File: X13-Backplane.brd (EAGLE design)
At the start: 101.6 x 139.3 mm, 38 parts, among them J1 PXC-PTSM-04-RA-1778641, J2 284512-4, J3 284512-8, J4 PXC-PTSM-04-RA-1778641, J5 PXC-PTSM-04-RA-1778641, J6 284512-4, J8 284512-8, T1 284512-3, T2 284512-3, T3 284512-3, T4 284512-3, T5 284512-3, T6 284512-3, T7 284512-3, T8 284512-3

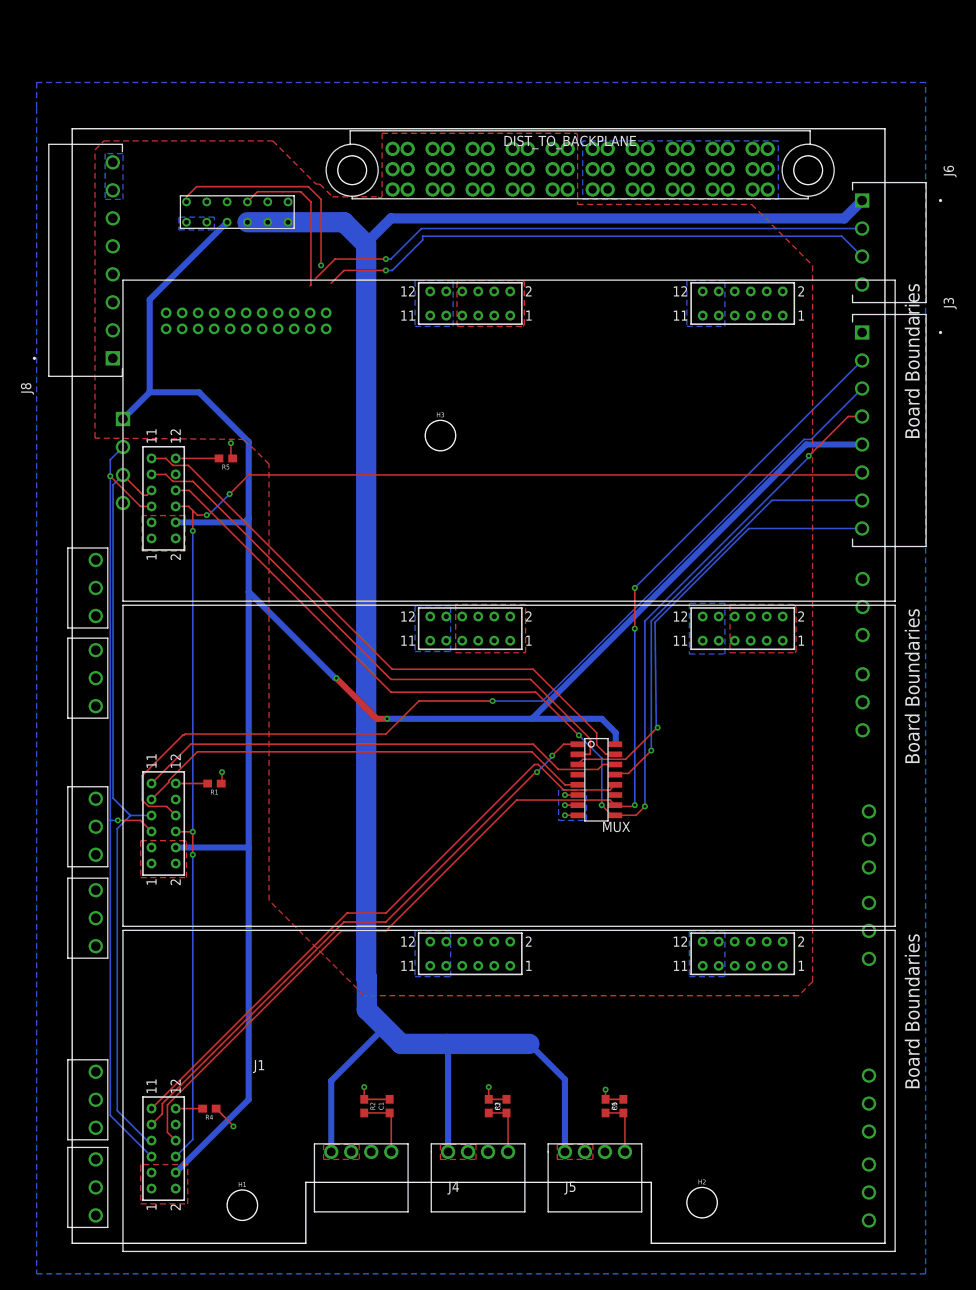
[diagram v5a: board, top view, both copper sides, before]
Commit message: updated board layout and connections
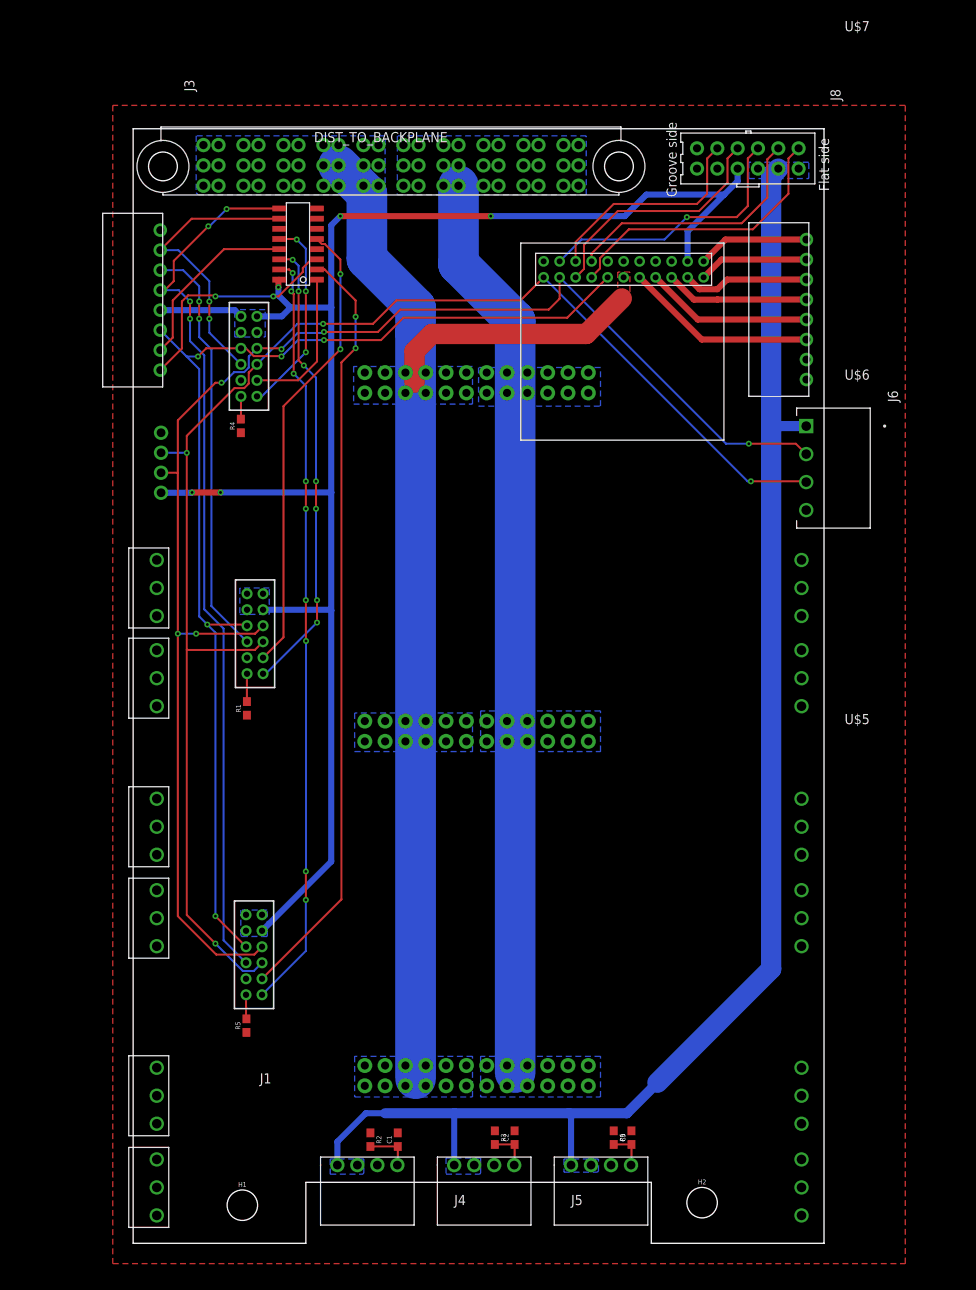
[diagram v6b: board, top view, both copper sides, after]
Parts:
- removed H3: 6-32-HOLE, Mounting Holes:6-32-HOLE
- added U$5, U$6, U$7: BACKPLANE_ESC_ADAPTER_PWRBKP, Backplane_ESC_adapter:BACKPLANE_ESC_ADAPTER_BKP_PWR
- DIST_LOGIC_TO_BACKPLANE: value IPL1-107-01-L-D-RE-P -> IPL1-106-01-L-D-K; device Backplane_Dist_Logic_Connector:IPL1-107-01-L-D-RE-P -> Backplane_Dist_Logic_Connector:IPL1-106-01-L-D-K
- J2: value 284512-4 -> PXC-PTSM-04-RA-1778641; device 284512-4:TE_284512-4 -> Phoenix Contact PTSM-04-V-1778573:PXC-PTSM-04-RA-1778641
- J3, J8: value 284512-8 -> PXC-8-RA-1778683; device 284512-8:TE_284512-8 -> Phoenix Contact PTSM 8 pin:PXC-8-RA-1778683
- U$1, U$2, U$3: value BACKPLANE_CONNECTORS -> BACKPLANE_CONNECTORSBKP; device BLHeli_32 45A:BACKPLANE_CONNECTORS -> BLHeli_32 45A:BACKPLANE_CONNECTORS_BKP
- moved U$3 101.8 mm to (22.7, 36.1)
- moved J3 98.7 mm to (3.81, 128.7)
- moved U$1 96.9 mm to (22.1, 110.9)
- moved R4 85.4 mm to (21.1, 102.2), turned to 90 degrees
- moved J8 79.6 mm to (84.6, 127.6), turned to 270 degrees
- moved R5 70.9 mm to (21.8, 27.2), turned to 90 degrees
- moved MUX 66.6 mm to (30.6, 120.5), turned to 180 degrees
- moved DIST_LOGIC_TO_BACKPLANE 64.2 mm to (90.8, 134.3)
- moved U$2 61.0 mm to (22.9, 76.2)
- moved U$4 47.9 mm to (78.9, 122.7), flipped to the top, turned to 180 degrees
- moved T2 35.3 mm to (93.2, 40.6)
- moved MC4 33.2 mm to (93.2, 6.99)
- moved J6 29.0 mm to (91.8, 96.9)
- moved DIST_TO_BACKPLANE 23.7 mm to (39.8, 139.5)
- moved R1 10.2 mm to (21.8, 66.9), turned to 90 degrees
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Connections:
- new net 12VGND: DIST_TO_BACKPLANE.1@1, DIST_TO_BACKPLANE.1@2, DIST_TO_BACKPLANE.1@3, DIST_TO_BACKPLANE.1@4, DIST_TO_BACKPLANE.1@5, DIST_TO_BACKPLANE.1@6, DIST_TO_BACKPLANE.2@1, DIST_TO_BACKPLANE.2@2, DIST_TO_BACKPLANE.2@3, DIST_TO_BACKPLANE.2@4, DIST_TO_BACKPLANE.2@5, DIST_TO_BACKPLANE.2@6, DIST_TO_BACKPLANE.3@1, DIST_TO_BACKPLANE.3@2, DIST_TO_BACKPLANE.3@3, DIST_TO_BACKPLANE.3@4, DIST_TO_BACKPLANE.3@5, DIST_TO_BACKPLANE.3@6, DIST_TO_BACKPLANE.4@1, DIST_TO_BACKPLANE.4@2, DIST_TO_BACKPLANE.4@3, DIST_TO_BACKPLANE.4@4, DIST_TO_BACKPLANE.4@5, DIST_TO_BACKPLANE.4@6, DIST_TO_BACKPLANE.5@1, DIST_TO_BACKPLANE.5@2, DIST_TO_BACKPLANE.5@3, DIST_TO_BACKPLANE.5@4, DIST_TO_BACKPLANE.5@5, DIST_TO_BACKPLANE.5@6, U$5.GND@1, U$5.GND@10, U$5.GND@11, U$5.GND@12, U$5.GND@2, U$5.GND@3, U$5.GND@4, U$5.GND@5, U$5.GND@6, U$5.GND@7, U$5.GND@8, U$5.GND@9, U$6.GND@1, U$6.GND@10, U$6.GND@11, U$6.GND@12, U$6.GND@2, U$6.GND@3, U$6.GND@4, U$6.GND@5, U$6.GND@6, U$6.GND@7, U$6.GND@8, U$6.GND@9, U$7.GND@1, U$7.GND@10, U$7.GND@11, U$7.GND@12, U$7.GND@2, U$7.GND@3, U$7.GND@4, U$7.GND@5, U$7.GND@6, U$7.GND@7, U$7.GND@8, U$7.GND@9
- net 12V: now also U$5.12V@1, U$5.12V@10, U$5.12V@11, U$5.12V@12, U$5.12V@2, U$5.12V@3, U$5.12V@4, U$5.12V@5, U$5.12V@6, U$5.12V@7, U$5.12V@8, U$5.12V@9, U$6.12V@1, U$6.12V@10, U$6.12V@11, U$6.12V@12, U$6.12V@2, U$6.12V@3, U$6.12V@4, U$6.12V@5, U$6.12V@6, U$6.12V@7, U$6.12V@8, U$6.12V@9, U$7.12V@1, U$7.12V@10, U$7.12V@11, U$7.12V@12, U$7.12V@2, U$7.12V@3, U$7.12V@4, U$7.12V@5, U$7.12V@6, U$7.12V@7, U$7.12V@8, U$7.12V@9; no longer U$1.1, U$1.13, U$1.14, U$1.15, U$1.16, U$1.17, U$1.18, U$1.19, U$1.2, U$1.20, U$1.3, U$1.4, U$1.5, U$1.6, U$1.7, U$1.8, U$2.1, U$2.13, U$2.14, U$2.15, U$2.16, U$2.17, U$2.18, U$2.19, U$2.2, U$2.20, U$2.3, U$2.4, U$2.5, U$2.6, U$2.7, U$2.8, U$3.1, U$3.13, U$3.14, U$3.15, U$3.16, U$3.17, U$3.18, U$3.19, U$3.2, U$3.20, U$3.3, U$3.4, U$3.5, U$3.6, U$3.7, U$3.8
- net 3.3V: now also U$1.1, U$1.2, U$1.3, U$1.4, U$2.1, U$2.2, U$2.3, U$2.4, U$3.1, U$3.2, U$3.3, U$3.4; no longer U$1.25, U$1.26, U$1.27, U$1.28, U$2.25, U$2.26, U$2.27, U$2.28, U$3.25, U$3.26, U$3.27, U$3.28
- net CAN_H: now also U$1.5, U$2.5, U$3.5; no longer U$1.29, U$2.29, U$3.29
- net CAN_L: now also U$1.7, U$2.7, U$3.7; no longer U$1.31, U$2.31, U$3.31
- net ESCID_1: now also U$1.12; no longer U$1.36
- net ESCID_2: now also U$2.12; no longer U$2.36
- net ESCID_3: now also U$3.12; no longer U$3.36
- net GND: no longer DIST_TO_BACKPLANE.1@1, DIST_TO_BACKPLANE.1@2, DIST_TO_BACKPLANE.1@3, DIST_TO_BACKPLANE.1@4, DIST_TO_BACKPLANE.1@5, DIST_TO_BACKPLANE.1@6, DIST_TO_BACKPLANE.2@1, DIST_TO_BACKPLANE.2@2, DIST_TO_BACKPLANE.2@3, DIST_TO_BACKPLANE.2@4, DIST_TO_BACKPLANE.2@5, DIST_TO_BACKPLANE.2@6, DIST_TO_BACKPLANE.3@1, DIST_TO_BACKPLANE.3@2, DIST_TO_BACKPLANE.3@3, DIST_TO_BACKPLANE.3@4, DIST_TO_BACKPLANE.3@5, DIST_TO_BACKPLANE.3@6, DIST_TO_BACKPLANE.4@1, DIST_TO_BACKPLANE.4@2, DIST_TO_BACKPLANE.4@3, DIST_TO_BACKPLANE.4@4, DIST_TO_BACKPLANE.4@5, DIST_TO_BACKPLANE.4@6, DIST_TO_BACKPLANE.5@1, DIST_TO_BACKPLANE.5@2, DIST_TO_BACKPLANE.5@3, DIST_TO_BACKPLANE.5@4, DIST_TO_BACKPLANE.5@5, DIST_TO_BACKPLANE.5@6, U$1.10, U$1.11, U$1.12, U$1.21, U$1.22, U$1.23, U$1.24, U$1.9, U$2.10, U$2.11, U$2.12, U$2.21, U$2.22, U$2.23, U$2.24, U$2.9, U$3.10, U$3.11, U$3.12, U$3.21, U$3.22, U$3.23, U$3.24, U$3.9
- net NRST: now also U$1.6, U$2.6, U$3.6; no longer U$1.30, U$2.30, U$3.30
- net PROG_1: now also U$1.8; no longer U$1.32
- net PROG_2: now also U$2.8; no longer U$2.32
- net PROG_3: now also U$3.8; no longer U$3.32
- net SWCLK_1: now also U$1.11; no longer U$1.35
- net SWCLK_2: now also U$2.11; no longer U$2.35
- net SWCLK_3: now also U$3.11; no longer U$3.35
- net SWDIO_1: now also U$1.9; no longer U$1.33
- net SWDIO_2: now also U$2.9; no longer U$2.33
- net SWDIO_3: now also U$3.9; no longer U$3.33
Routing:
- net 12V: track 0.00 -> 152.4 mm
- net 12VGND: track 0.00 -> 113.8 mm
- net PROG_1: track 146.8 -> 36.3 mm, vias 3 -> 2
- net PROG_2: track 118.1 -> 52.6 mm, vias 1 -> 2
- net 5V: track 244.2 -> 183.9 mm
- net 3.3V: track 268.5 -> 210.8 mm, vias 2 -> 5
- net SWDIO_1: track 73.8 -> 18.8 mm, vias 2 -> 0
- net SWCLK_1: track 77.3 -> 25.2 mm, vias 0 -> 3
- net C2_2: track 0.00 -> 35.9 mm
- net C2_1: track 0.00 -> 32.6 mm
- net SWCLK_IN: track 54.6 -> 22.8 mm, vias 1 -> 0
- net ALERT_2: track 0.00 -> 30.5 mm
- net PROG_3: track 140.4 -> 110.5 mm
- net NRST: track 172.3 -> 144.1 mm
- net ALERT_1: track 0.00 -> 27.6 mm
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- added copper zone on layer 16, net 12V
- added copper zone on layer 16, net 12VGND
- added copper zone on layer 16, net 3.3V
- added copper zone on layer 16, net 5V
- added copper zone on layer 1, net GND
- removed copper zone on layer 1, net 3.3V
- removed copper zone on layer 1, net 5V
- removed copper zone on layer 16, net GND
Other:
- board size 101.6 x 139.3 mm -> 86.4 x 139.3 mm

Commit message: updated board layout and connections
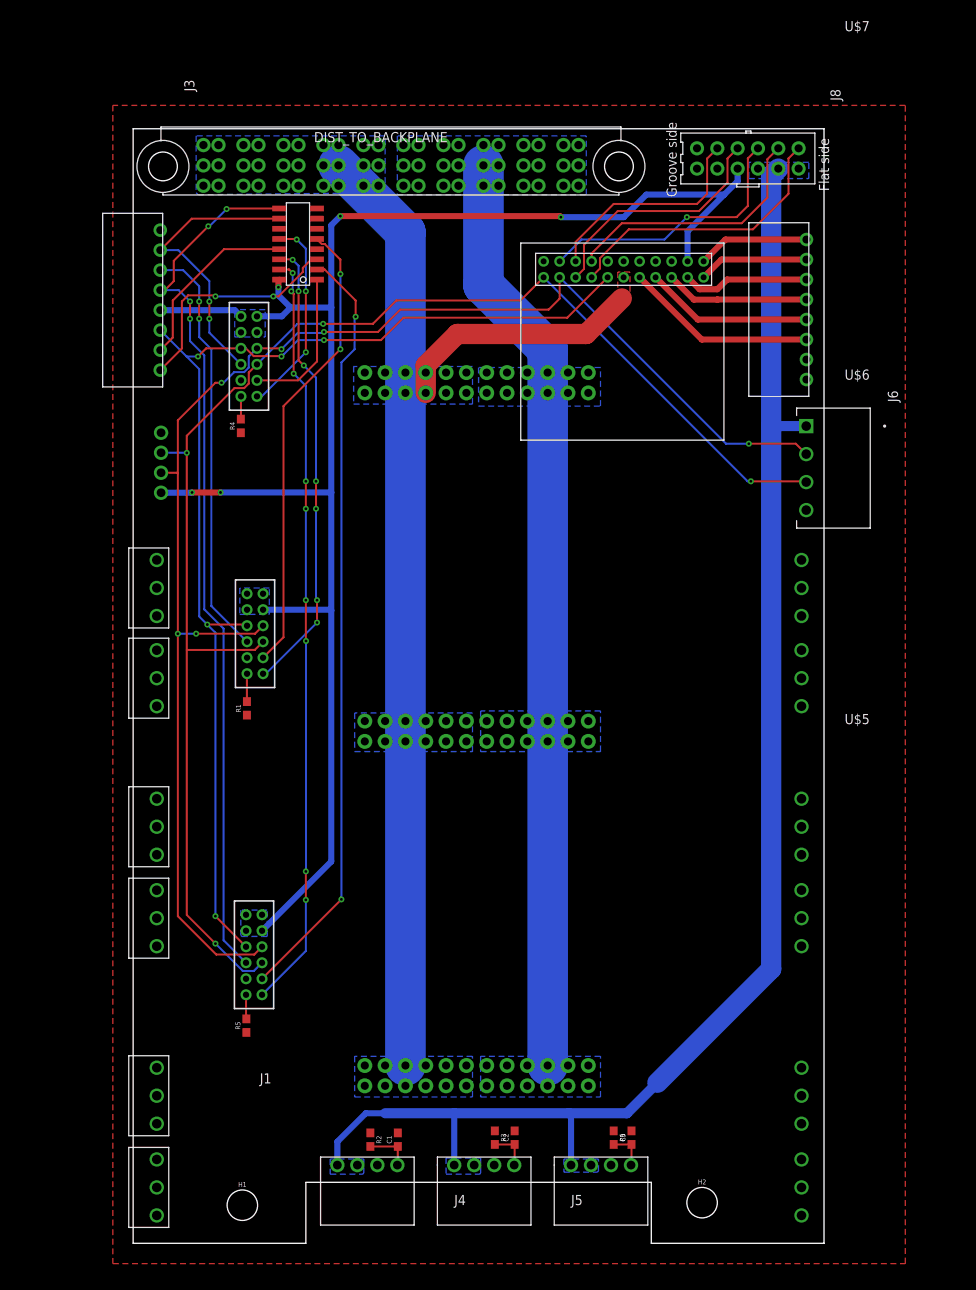
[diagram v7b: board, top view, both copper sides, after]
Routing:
- net 12V: track 152.4 -> 147.4 mm
- net 12VGND: track 113.8 -> 115.8 mm

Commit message: updated board
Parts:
- removed MC1, MC2, MC3, MC4, T1, T2, T3, T4, T5, T6, T7, T8: 284512-3, ThrusterConnector:284512-3
- added C4: .1uF, SparkFun-Capacitors:0603
- added C5: 47uF, Panasonic 47 uF cap - EEE-1CA470SP:PANASONIC_D
- added D1, D2, D3, D4: 0.5A/40V/420mV, SparkFun-DiscreteSemi:SOD-323
- added R7, R8: 60, SparkFun-Resistors:0603
- moved J8 26.1 mm to (99.1, 105.9), turned to 90 degrees
- moved J6 20.6 mm to (91.6, 76.3)
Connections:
- removed net DATA1: U$4.22
- removed net MC1_PHS1: MC1.1
- removed net MC1_PHS2: MC1.2
- removed net MC1_PHS3: MC1.3
- removed net MC2_PHS1: MC2.1
- removed net MC2_PHS2: MC2.2
- removed net MC2_PHS3: MC2.3
- removed net MC3_PHS1: MC3.1
- removed net MC3_PHS2: MC3.2
- removed net MC3_PHS3: MC3.3
- removed net MC4_PHS1: MC4.1
- removed net MC4_PHS2: MC4.2
- removed net MC4_PHS3: MC4.3
- removed net T1_PHS1: T1.1
- removed net T1_PHS2: T1.2
- removed net T1_PHS3: T1.3
- removed net T2_PHS1: T2.1
- removed net T2_PHS2: T2.2
- removed net T2_PHS3: T2.3
- removed net T3_PHS1: T3.1
- removed net T3_PHS2: T3.2
- removed net T3_PHS3: T3.3
- removed net T4_PHS1: T4.1
- removed net T4_PHS2: T4.2
- removed net T4_PHS3: T4.3
- removed net T5_PHS1: T5.1
- removed net T5_PHS2: T5.2
- removed net T5_PHS3: T5.3
- removed net T6_PHS1: T6.1
- removed net T6_PHS2: T6.2
- removed net T6_PHS3: T6.3
- removed net T7_PHS1: T7.1
- removed net T7_PHS2: T7.2
- removed net T7_PHS3: T7.3
- removed net T8_PHS1: T8.1
- removed net T8_PHS2: T8.2
- removed net T8_PHS3: T8.3
- new net N$3: C4.1, R7.1, R8.2
- new net NRST_1: D1.A, U$1.6
- new net NRST_2: D2.A, U$2.6
- new net NRST_3: D3.A, U$3.6
- new net NRST_4: D4.A, U$4.13
- net 12V: now also C5.+, J8.1, J8.2
- net CAN_H: now also R7.2
- net CAN_L: now also R8.1
- net DATA: now also U$4.22
- net GND: now also C4.2, C5.-; no longer J8.7, J8.8
- net NRST: now also D1.C, D2.C, D3.C, D4.C; no longer U$1.6, U$2.6, U$3.6, U$4.13
- net PROG_1: no longer U$1.8
- net PROG_2: no longer U$2.8
- net PROG_3: no longer U$3.8
- net SOL1_1: now also J8.8; no longer J8.1
- net SOL2_1: now also J8.7; no longer J8.2
- net SOL3_1: now also J8.6; no longer J8.3
- net SOL4_1: now also J8.5; no longer J8.4
- net SOL5_1: now also J8.4; no longer J8.5
- net SOL6_1: now also J8.3; no longer J8.6
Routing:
- net PROG_3: track 110.5 -> 20.6 mm, vias 4 -> 2
- net PROG_2: track 52.6 -> 0.00 mm, vias 2 -> 0
- net NRST: track 144.1 -> 100.0 mm, vias 5 -> 6
- net 12V: track 147.4 -> 179.4 mm
- net NRST_4: track 0.00 -> 31.3 mm, vias 0 -> 1
- net DATA: track 0.00 -> 25.0 mm
- net CAN_L: track 182.9 -> 203.0 mm, vias 4 -> 5
- net PROG_1: track 36.3 -> 16.5 mm, vias 2 -> 0
- net CAN_H: track 185.6 -> 201.8 mm
- net 3.3V: track 210.9 -> 226.2 mm
- net NRST_3: track 0.00 -> 6.78 mm
- net N$3: track 0.00 -> 5.02 mm
- net NRST_2: track 0.00 -> 2.99 mm
- net NRST_1: track 0.00 -> 2.64 mm
- net 12VGND: track 115.8 -> 113.3 mm
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- added copper zone on layer 1, net 12VGND
- added copper zone on layer 16, net GND
